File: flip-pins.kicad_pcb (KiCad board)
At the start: 2 copper layers, 3 parts

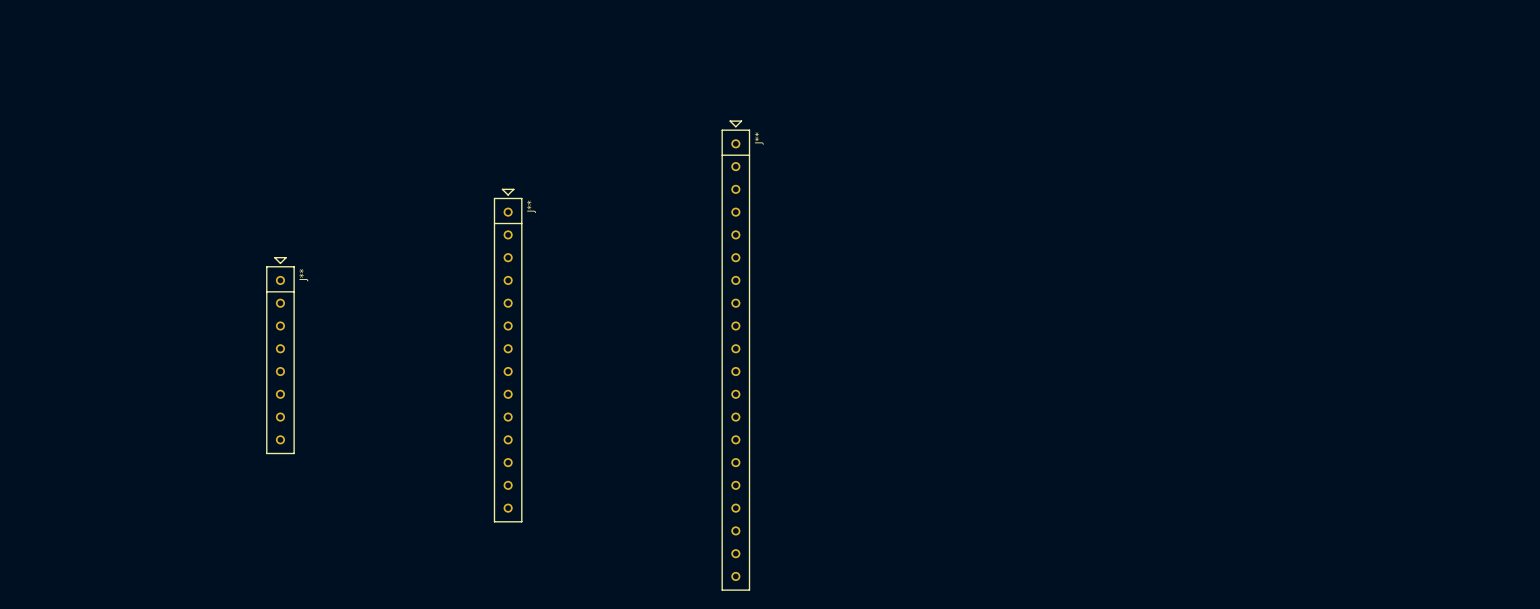
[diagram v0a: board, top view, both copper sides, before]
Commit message: added separate schematic, footprint, 3D versions of floating and aligner pins
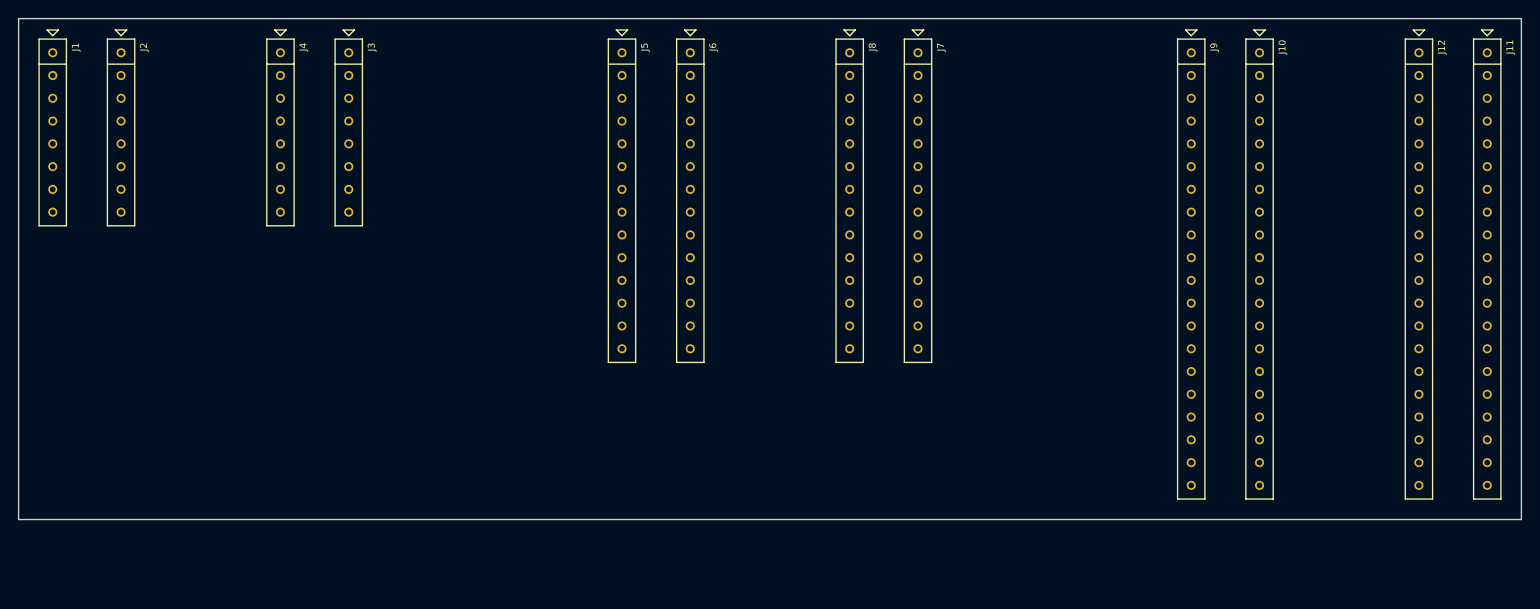
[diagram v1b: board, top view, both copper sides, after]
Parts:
- removed J**: FLIP-PINS-08, flip-pins:FLIP-PINS-08
- removed J**: FLIP-PINS-14, flip-pins:FLIP-PINS-14
- removed J**: FLIP-PINS-20, flip-pins:FLIP-PINS-20
- added J1: FLIP-PINS-ALIGN-08, flip-pins:FLIP-PINS-ALIGN-08, F.Cu at (50.8, 50.8)
- added J10: FLIP-PINS-ALIGN-20, flip-pins:FLIP-PINS-ALIGN-20, F.Cu at (185.4, 66.0)
- added J11: FLIP-PINS-FLOAT-20, flip-pins:FLIP-PINS-FLOAT-20, F.Cu at (210.8, 66.0)
- added J12: FLIP-PINS-FLOAT-20, flip-pins:FLIP-PINS-FLOAT-20, F.Cu at (203.2, 66.0)
- added J2: FLIP-PINS-ALIGN-08, flip-pins:FLIP-PINS-ALIGN-08, F.Cu at (58.4, 50.8)
- added J3: FLIP-PINS-FLOAT-08, flip-pins:FLIP-PINS-FLOAT-08, F.Cu at (83.8, 50.8)
- added J4: FLIP-PINS-FLOAT-08, flip-pins:FLIP-PINS-FLOAT-08, F.Cu at (76.2, 50.8)
- added J5: FLIP-PINS-ALIGN-14, flip-pins:FLIP-PINS-ALIGN-14, F.Cu at (114.3, 58.4)
- added J6: FLIP-PINS-ALIGN-14, flip-pins:FLIP-PINS-ALIGN-14, F.Cu at (121.9, 58.4)
- added J7: FLIP-PINS-FLOAT-14, flip-pins:FLIP-PINS-FLOAT-14, F.Cu at (147.3, 58.4)
- added J8: FLIP-PINS-FLOAT-14, flip-pins:FLIP-PINS-FLOAT-14, F.Cu at (139.7, 58.4)
- added J9: FLIP-PINS-ALIGN-20, flip-pins:FLIP-PINS-ALIGN-20, F.Cu at (177.8, 66.0)
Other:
- board outline added: 167.6 x 55.9 mm
